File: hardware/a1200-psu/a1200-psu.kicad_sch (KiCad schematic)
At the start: 62 parts, among them J1 220V, J2 Conn_01x05, Q1 P2N60, SW1 SW_SPST, U1 UC3844_DIP8, U2 PC817, U3 TL431D

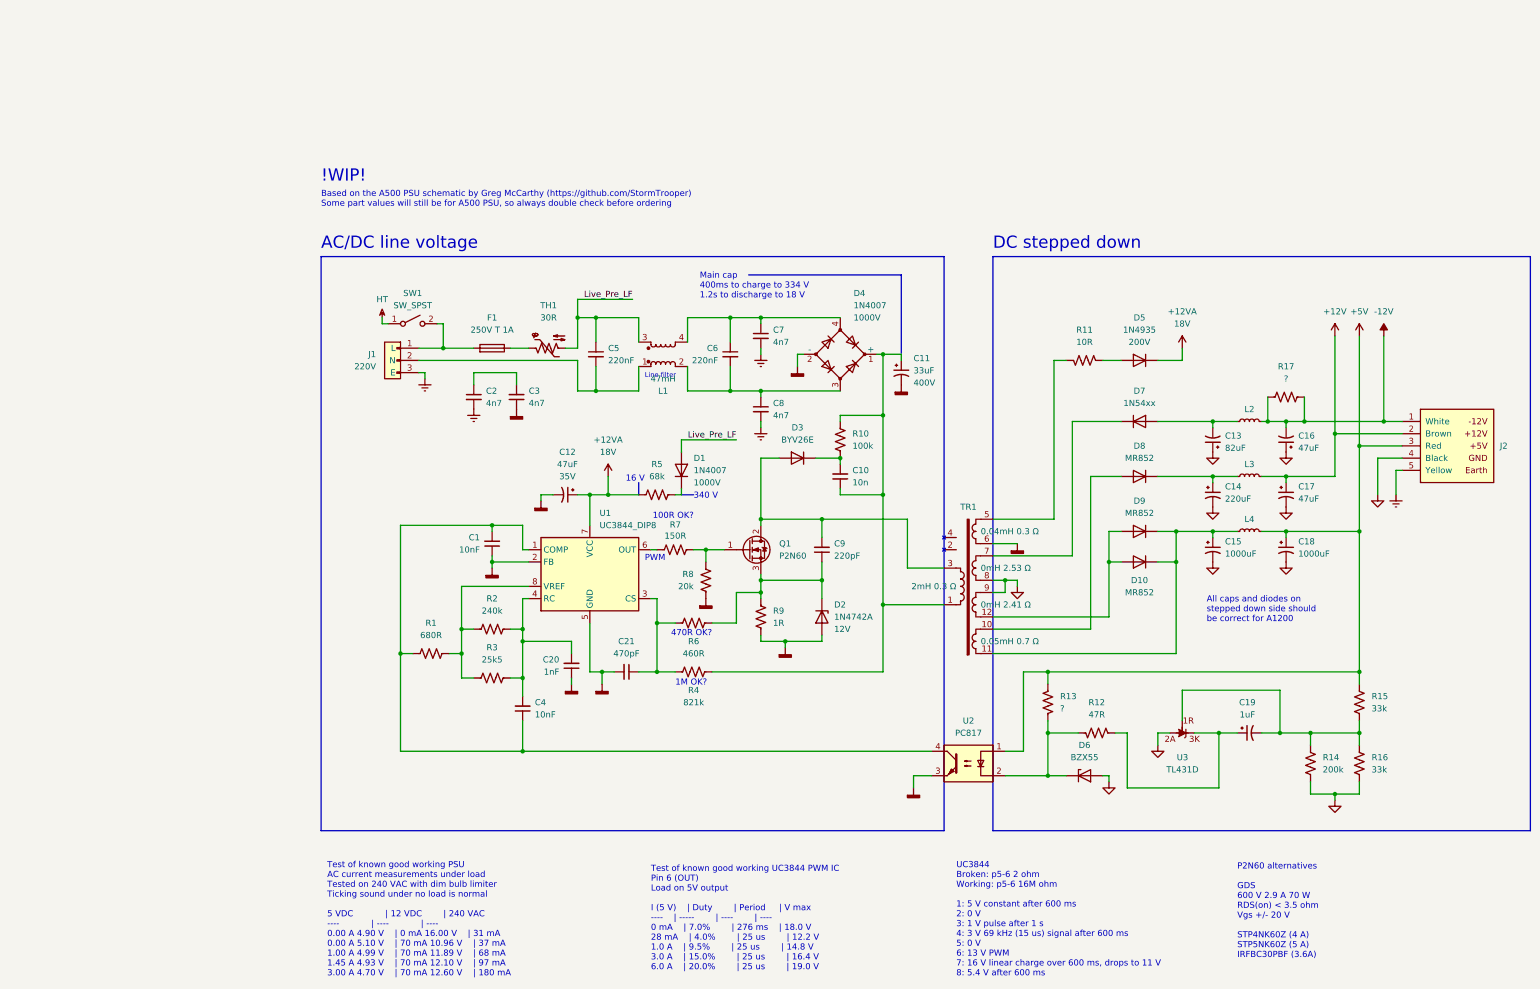
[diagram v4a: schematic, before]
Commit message: Fixed ERC/DRC errors
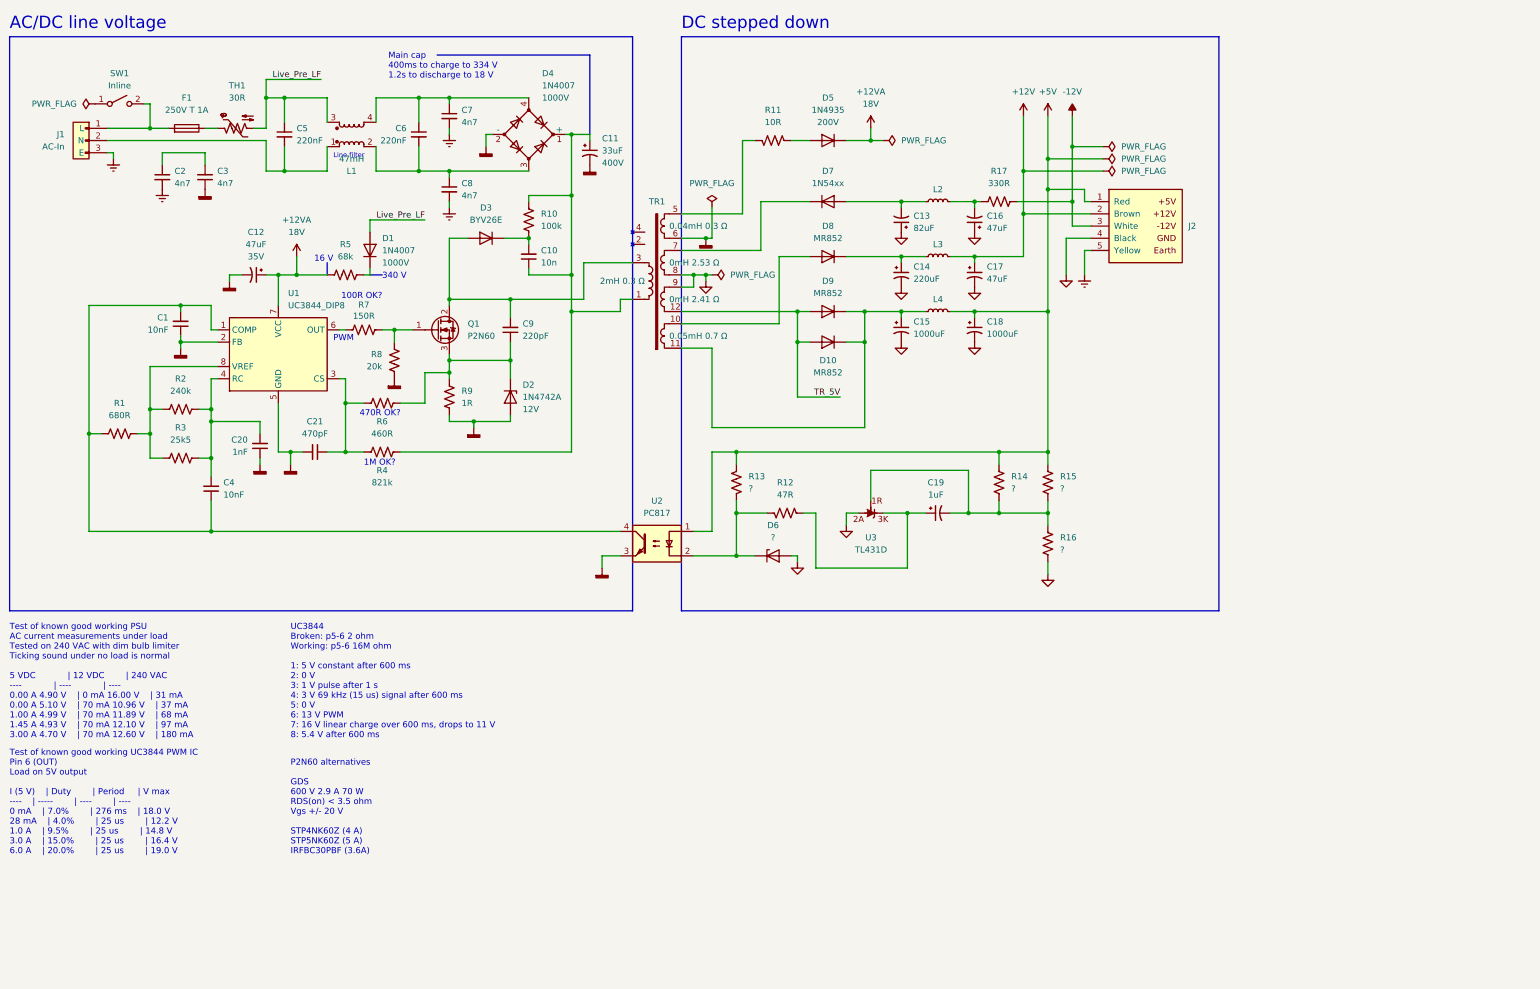
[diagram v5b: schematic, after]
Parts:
- C11, C12, C13, C14, C15, C16, C17, C18, C19: symbol a500-psu-rescue:CP1_Small-Device -> Device:C_Polarized_Small_US
- D10, D9: footprint Diode_THT:D_5W_P12.70mm_Horizontal -> Amiga 1200:Diode_Heatsink
- D6: value BZX55 -> ?
- J1: value 220V -> AC-In; now in the parts list
- J2: value Conn_01x05 -> DC-Out
- R14: value 200k -> ?
- R15, R16: value 33k -> ?
- R17: value ? -> 330R
- SW1: value SW_SPST -> Inline
- U3: footprint Package_TO_SOT_THT:TO-92 -> Package_TO_SOT_THT:TO-92_Wide
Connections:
- net +5V: now also J2.1 (Red), R14.2; no longer J2.3 (Red)
- net -12V: now also J2.3 (White); no longer C16.2, J2.1 (White), L2.2, R17.2
- net GND: no longer R14.1
- net TR_5V: now reaches D10.2 (A), D9.2 (A), TR1.12
- net at C19.2, R15.1, R16.2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: now also R14.1; no longer R14.2
- net HT: no longer names the net of SW1.1 (A)
- new net: C16.2, L2.2, R17.2
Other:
- note removed: "!WIP!"
- note removed: "All caps and diodes on stepped down side should be correct for A1200"
- note removed: "Based on the A500 PSU schematic by Greg McCarthy (https://github.com/StormTrooper) Some part values will still be for A500 PSU, so always double check before ordering"
- moved on the sheet: C1, C10, C11, C12, C13, C14, C15, C16, C17, C18, C19, C2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

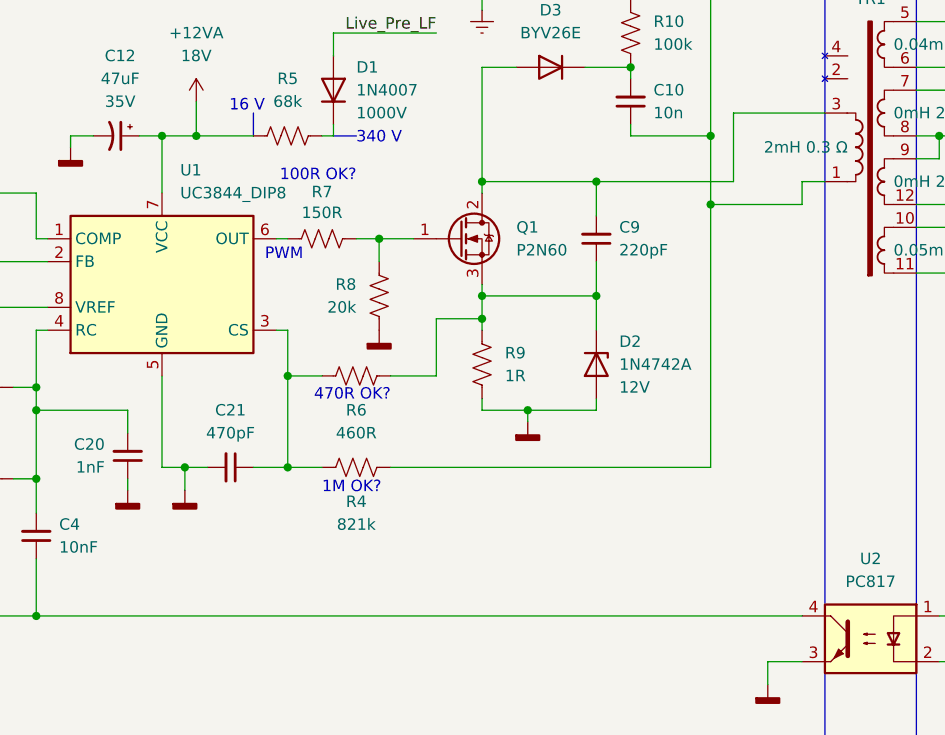
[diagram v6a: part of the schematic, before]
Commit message: Add warning for UC3844 pin 3 cap
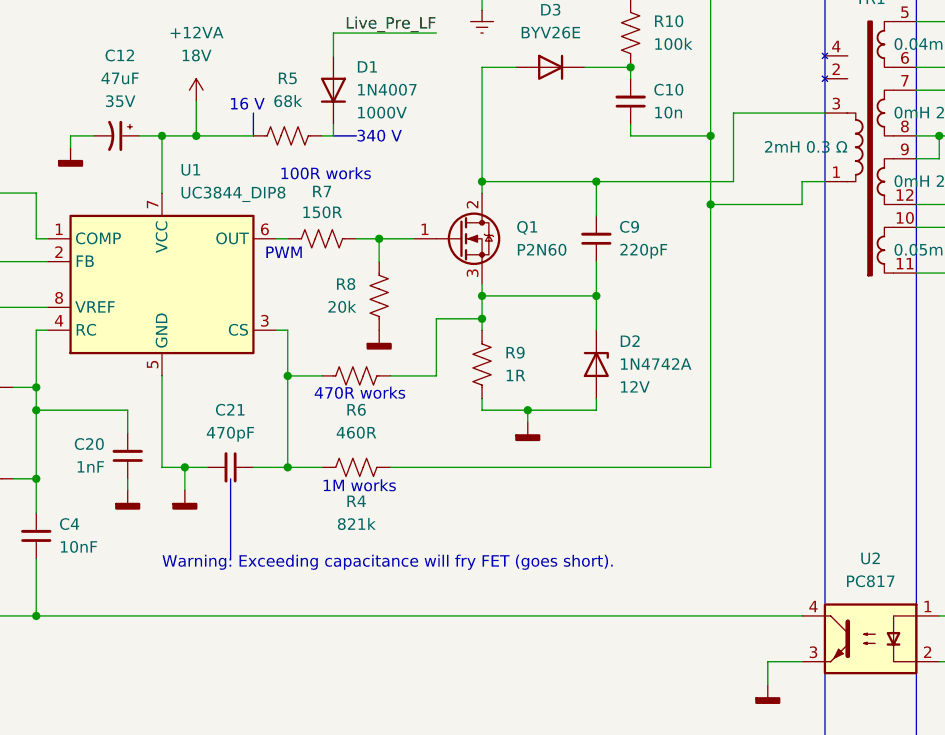
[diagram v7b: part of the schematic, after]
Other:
- note added: "100R works"
- note added: "1M works"
- note added: "470R works"
- note added: "Warning: Exceeding capacitance will fry FET (goes short)."
- note removed: "100R OK?"
- note removed: "1M OK?"
- note removed: "470R OK?"
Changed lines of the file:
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@@
     (title "Amiga A1200 PSU (UK)")
     (date "2023-02-11")
-    (rev "1G")
+    (rev "1H")
     (company "Nick Bolton")
     (comment 1 "Based on the A500 PSU schematic by Greg McCarthy")
@@
     (stroke (width 0) (type default) (color 0 0 0 0))
   )
+  (polyline (pts (xy 85.09 111.76) (xy 85.09 120.65))
+    (stroke (width 0) (type default) (color 0 0 0 0))
+  )
   (polyline (pts (xy 151.13 24.13) (xy 151.13 143.51))
     (stroke (width 0) (type default) (color 0 0 0 0))
@@
     (effects (font (size 1.27 1.27)) (justify left bottom))
   )
+  (text "Warning: Exceeding capacitance will fry FET (goes short)."
+    (at 77.47 121.92 0)
+    (effects (font (size 1.27 1.27)) (justify left bottom))
+  )
   (text "16 V" (at 88.9 71.12 180)
     (effects (font (size 1.27 1.27)) (justify right bottom))
@@
     (effects (font (size 2.54 2.54)) (justify left bottom))
   )
-  (text "100R OK?" (at 90.551 78.867 0)
+  (text "100R works" (at 90.551 78.867 0)
     (effects (font (size 1.27 1.27)) (justify left bottom))
   )
@@
     (effects (font (size 1.27 1.27)) (justify left bottom))
   )
-  (text "470R OK?" (at 94.361 103.251 0)
+  (text "470R works" (at 94.361 103.251 0)
     (effects (font (size 1.27 1.27)) (justify left bottom))
   )
@@
     (effects (font (size 1.27 1.27)) (justify left bottom))
   )
-  (text "1M OK?" (at 95.25 113.538 0)
+  (text "1M works" (at 95.25 113.538 0)
     (effects (font (size 1.27 1.27)) (justify left bottom))
   )

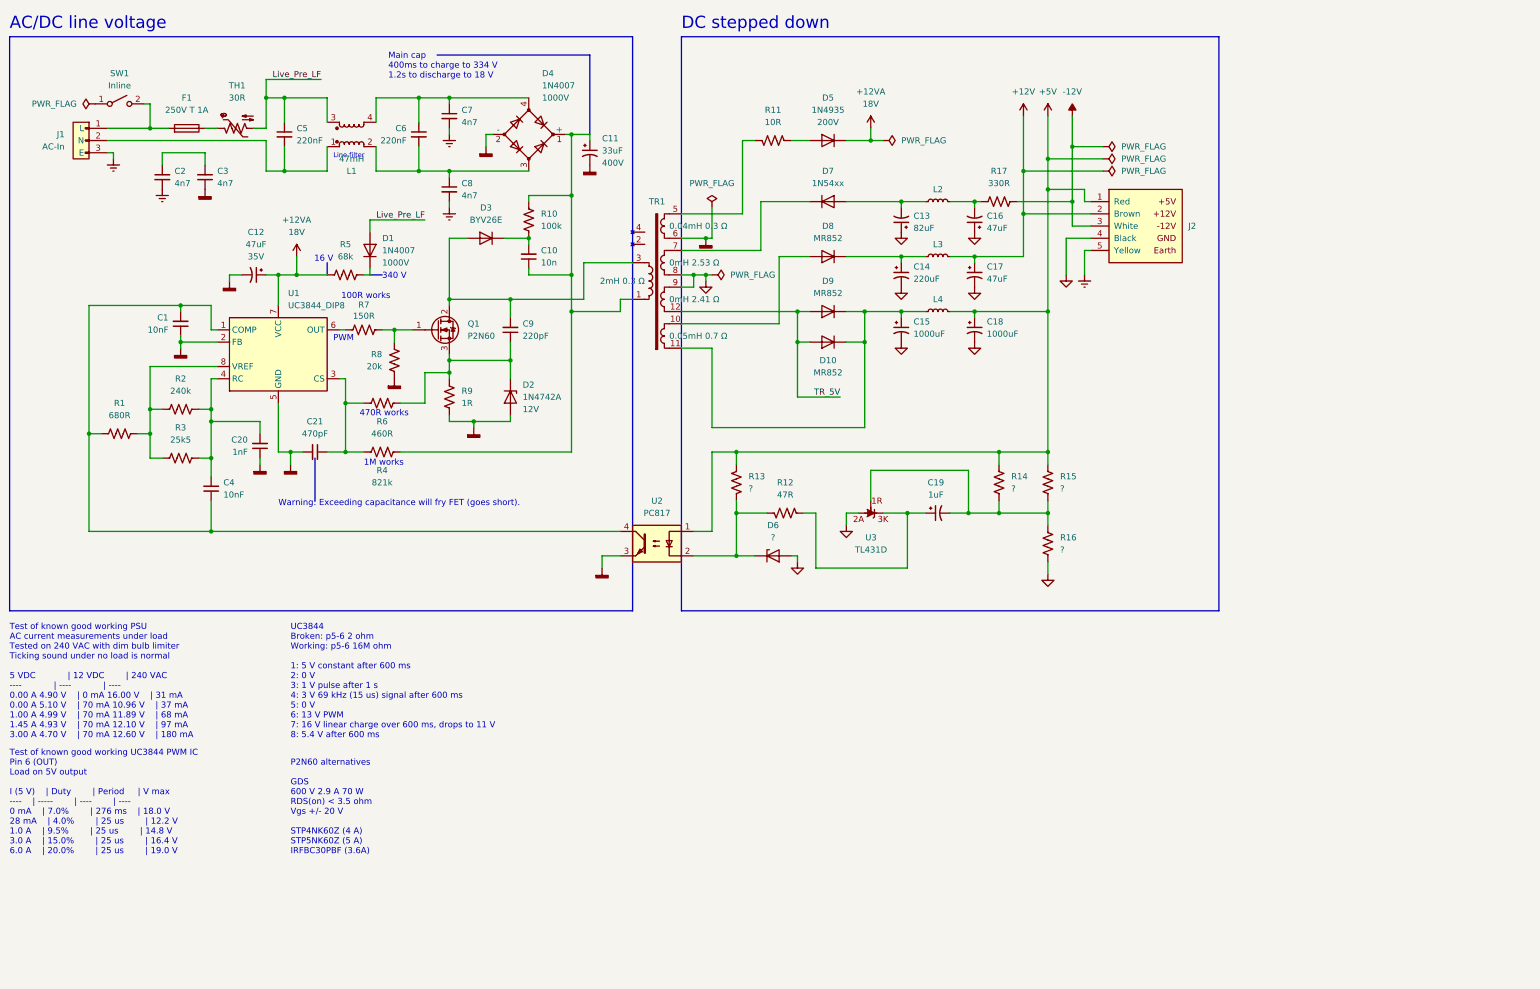
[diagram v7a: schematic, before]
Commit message: Reorganised PWM IC power supply
Also discovered some new part values
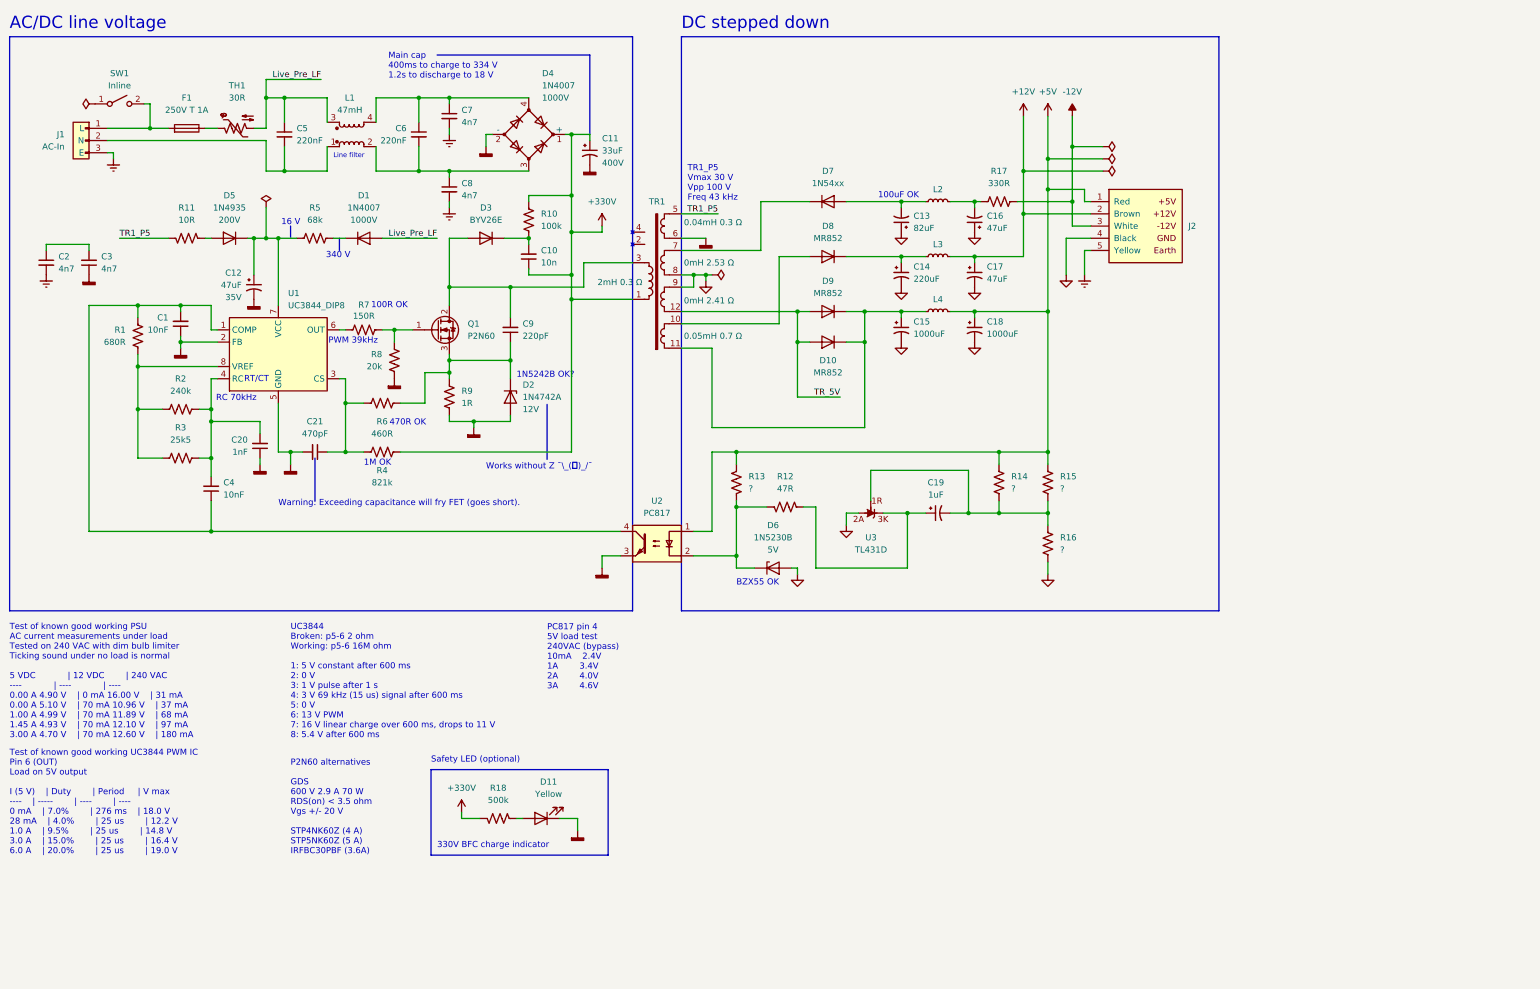
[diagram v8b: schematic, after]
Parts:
- added D11: Yellow, LED_THT:LED_D3.0mm, symbol Device:LED
- added R18: 500k, Resistor_THT:R_Axial_DIN0207_L6.3mm_D2.5mm_P10.16mm_Horizontal, symbol Device:R_US
- D4: symbol Device:D_Bridge_+-AA -> Amiga 1200:D_Bridge
- D6: value ? -> 1N5230B; Vz (none) -> 5V
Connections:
- net GNDD: now also D11.1 (K)
- net at R2.1, R3.1, U1.8 (VREF): now also R1.2; no longer R1.1
- net at C1.2, C4.1, U1.1 (COMP)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: now also R1.1; no longer R1.2
- net +330V: now reaches C10.1, C11.1, D4.1 (+), R10.1, R4.1, TR1.1
- net +330V: now also R18.2
- net TR1_P5: now reaches R11.2, TR1.5
- net +12VA: no longer names the net of C12.1, D5.1 (K), R5.1, U1.7 (VCC)
- new net: D11.2 (A), R18.1
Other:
- note added: "100R OK"
- note added: "100uF OK"
- note added: "1M OK"
- note added: "1N5242B OK?"
- note added: "330V BFC charge indicator"
- note added: "470R OK"
- note added: "BZX55 OK"
- note added: "PC817 pin 4 5V load test 240VAC (bypass) 10mA 2.4V 1A 3.4V 2A 4.0V 3A 4.6V"
- note added: "PWM 39kHz"
- note added: "RC 70kHz"
- note added: "RT/CT"
- note added: "Safety LED (optional)"
- note added: "TR1_P5 Vmax 30 V Vpp 100 V Freq 43 kHz"
- note added: "Works without Z ¯\_(ツ)_/¯"
- note removed: "100R works"
- note removed: "1M works"
- note removed: "470R works"
- note removed: "PWM"
- moved on the sheet: C2, C3, D1, D6, R12, R5
